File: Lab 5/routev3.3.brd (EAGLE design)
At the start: 100 x 80 mm, 48 parts, among them J1 FTDI_DEVICERA_SMT, M1 WIRELESS-NRF24L01, U1 3.3V, U2 GY-521MPU6050

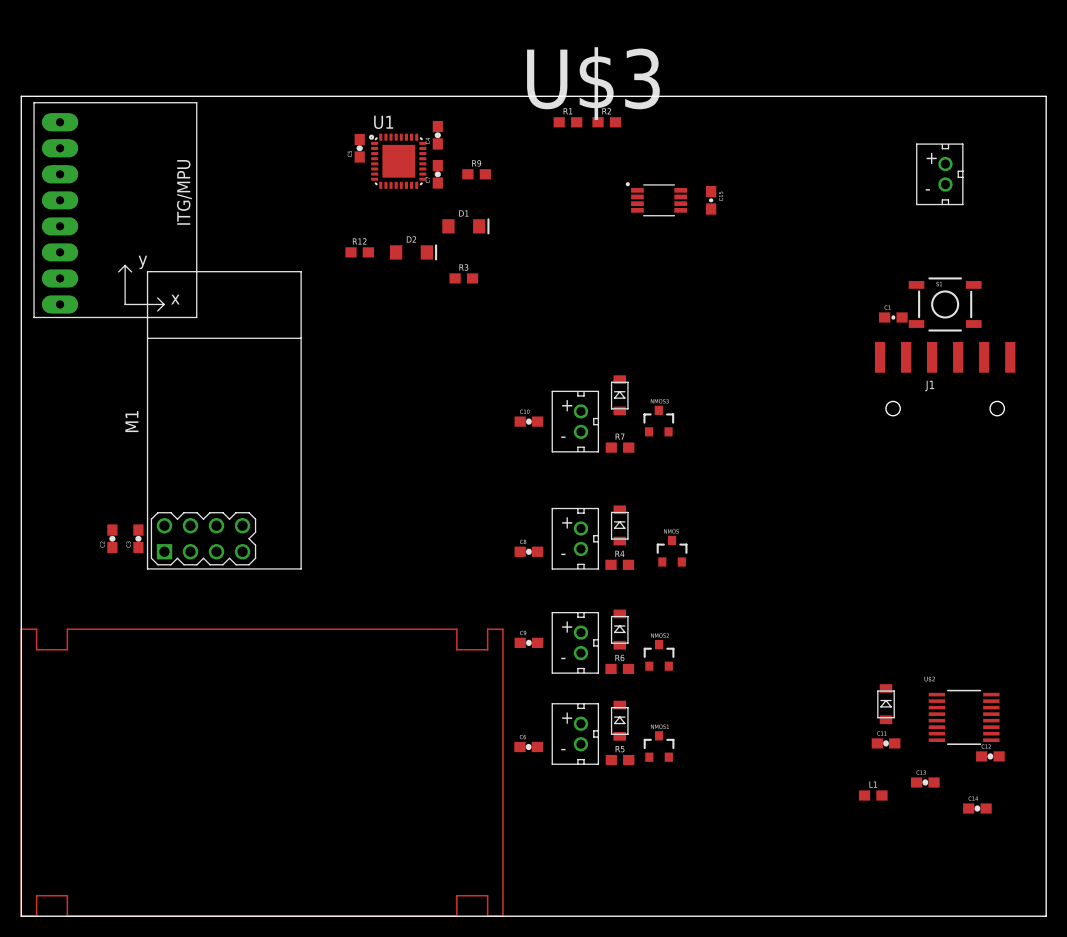
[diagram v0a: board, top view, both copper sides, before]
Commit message: Update template for cut-out - Latest route: routev3.5_vccgnd
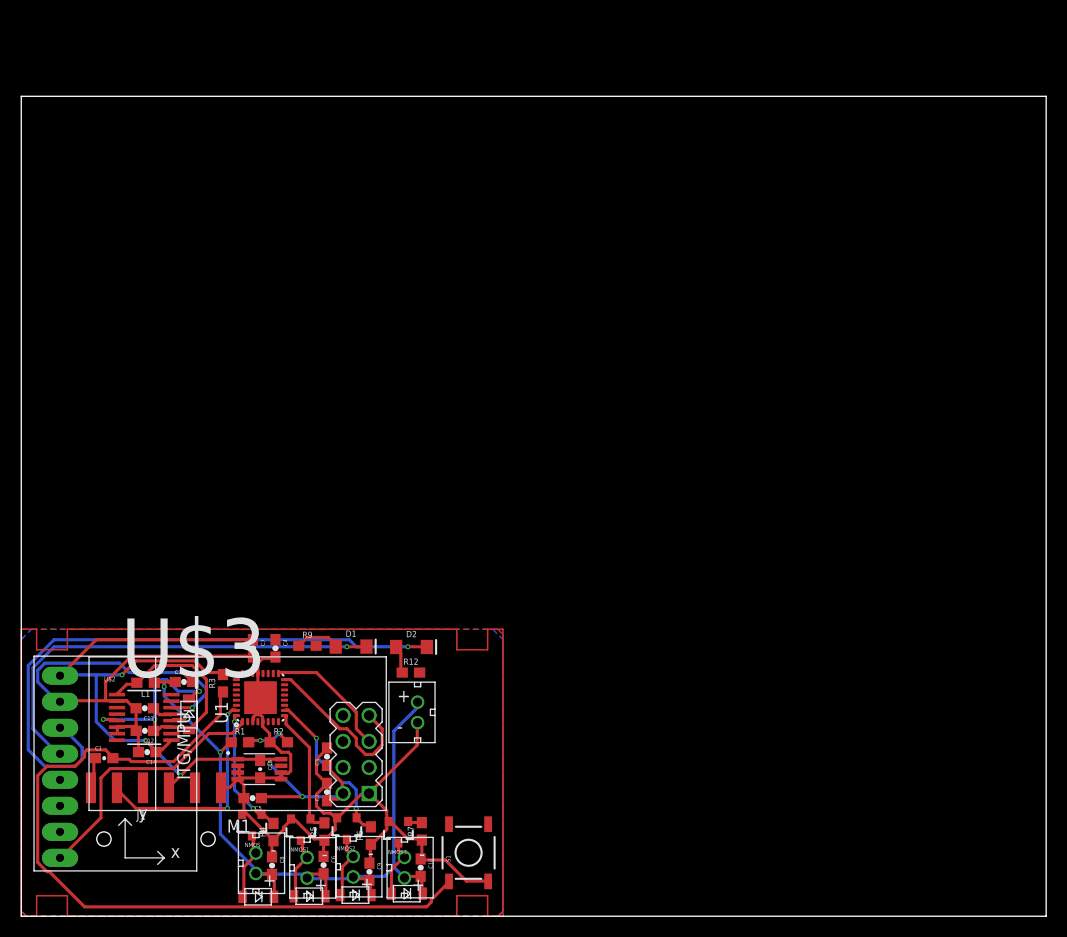
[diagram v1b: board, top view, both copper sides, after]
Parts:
- moved C1 88.2 mm to (8.09, 15.4)
- moved J1 87.7 mm to (13.1, 7.53)
- moved C12 82.5 mm to (12.1, 18.1), turned to 180 degrees
- moved C14 81.2 mm to (12.3, 16.0), turned to 180 degrees
- moved U$2 80.0 mm to (12.0, 19.4)
- moved C13 76.5 mm to (12.1, 20.3), turned to 180 degrees
- moved U$1 73.5 mm to (38.7, 19.9)
- moved L1 71.8 mm to (12.1, 22.8), turned to 180 degrees
- moved S1 70.9 mm to (43.6, 6.19), turned to 90 degrees
- moved C15 70.8 mm to (23.3, 14.3)
- moved C11 68.8 mm to (15.9, 22.9)
- moved R1 68.4 mm to (21.3, 17.0)
- moved R2 68.4 mm to (25.1, 17.0)
- moved DIODE4 68.0 mm to (16.4, 19.7)
- moved U$3 67.8 mm to (23.2, 14.3)
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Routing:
- net GND: track 0.00 -> 151.6 mm, vias 0 -> 2
- net VCC: track 0.00 -> 86.7 mm, vias 0 -> 5
- net RESET: track 0.00 -> 75.4 mm
- net BATTERY+: track 0.00 -> 75.3 mm, vias 0 -> 3
- net IMU-SCL: track 0.00 -> 58.9 mm, vias 0 -> 1
- net IMU-SDA: track 0.00 -> 43.0 mm, vias 0 -> 1
- net IMU-INT: track 0.00 -> 25.7 mm
- net FTDI-TX: track 0.00 -> 21.9 mm, vias 0 -> 2
- net VR-PS: track 0.00 -> 18.9 mm, vias 0 -> 3
- net RF-MISO: track 0.00 -> 16.7 mm
- net N$1: track 0.00 -> 16.1 mm
- net MOTOR3: track 0.00 -> 15.9 mm, vias 0 -> 2
- net MOTOR1: track 0.00 -> 12.7 mm, vias 0 -> 2
- net MOTOR2: track 0.00 -> 12.6 mm
- net RF-SCK: track 0.00 -> 12.6 mm
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- added copper zone on layer 1, net BATTERY_+
- added copper zone on layer 16, net GND
